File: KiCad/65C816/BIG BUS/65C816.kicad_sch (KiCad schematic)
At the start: 34 parts, among them J1 Displays, J2 Serial I/O, J3 Bus Header, J4 Bus Header, J5 Bus Header, J6 Bus Header, J7 Bus Header, J8 Bus Header, J9 PWR IN, SW2 RESET, SW3 PWR_ON, U1 W65C816SxP, U10 74LS109, U2 HM62256BLP, U3 74HC00, U4 28C256, U5 ATF16V8B, U6 74HC245, U7 74LS573, U8 NE555P, U9 74LS109, Y1 16MHz

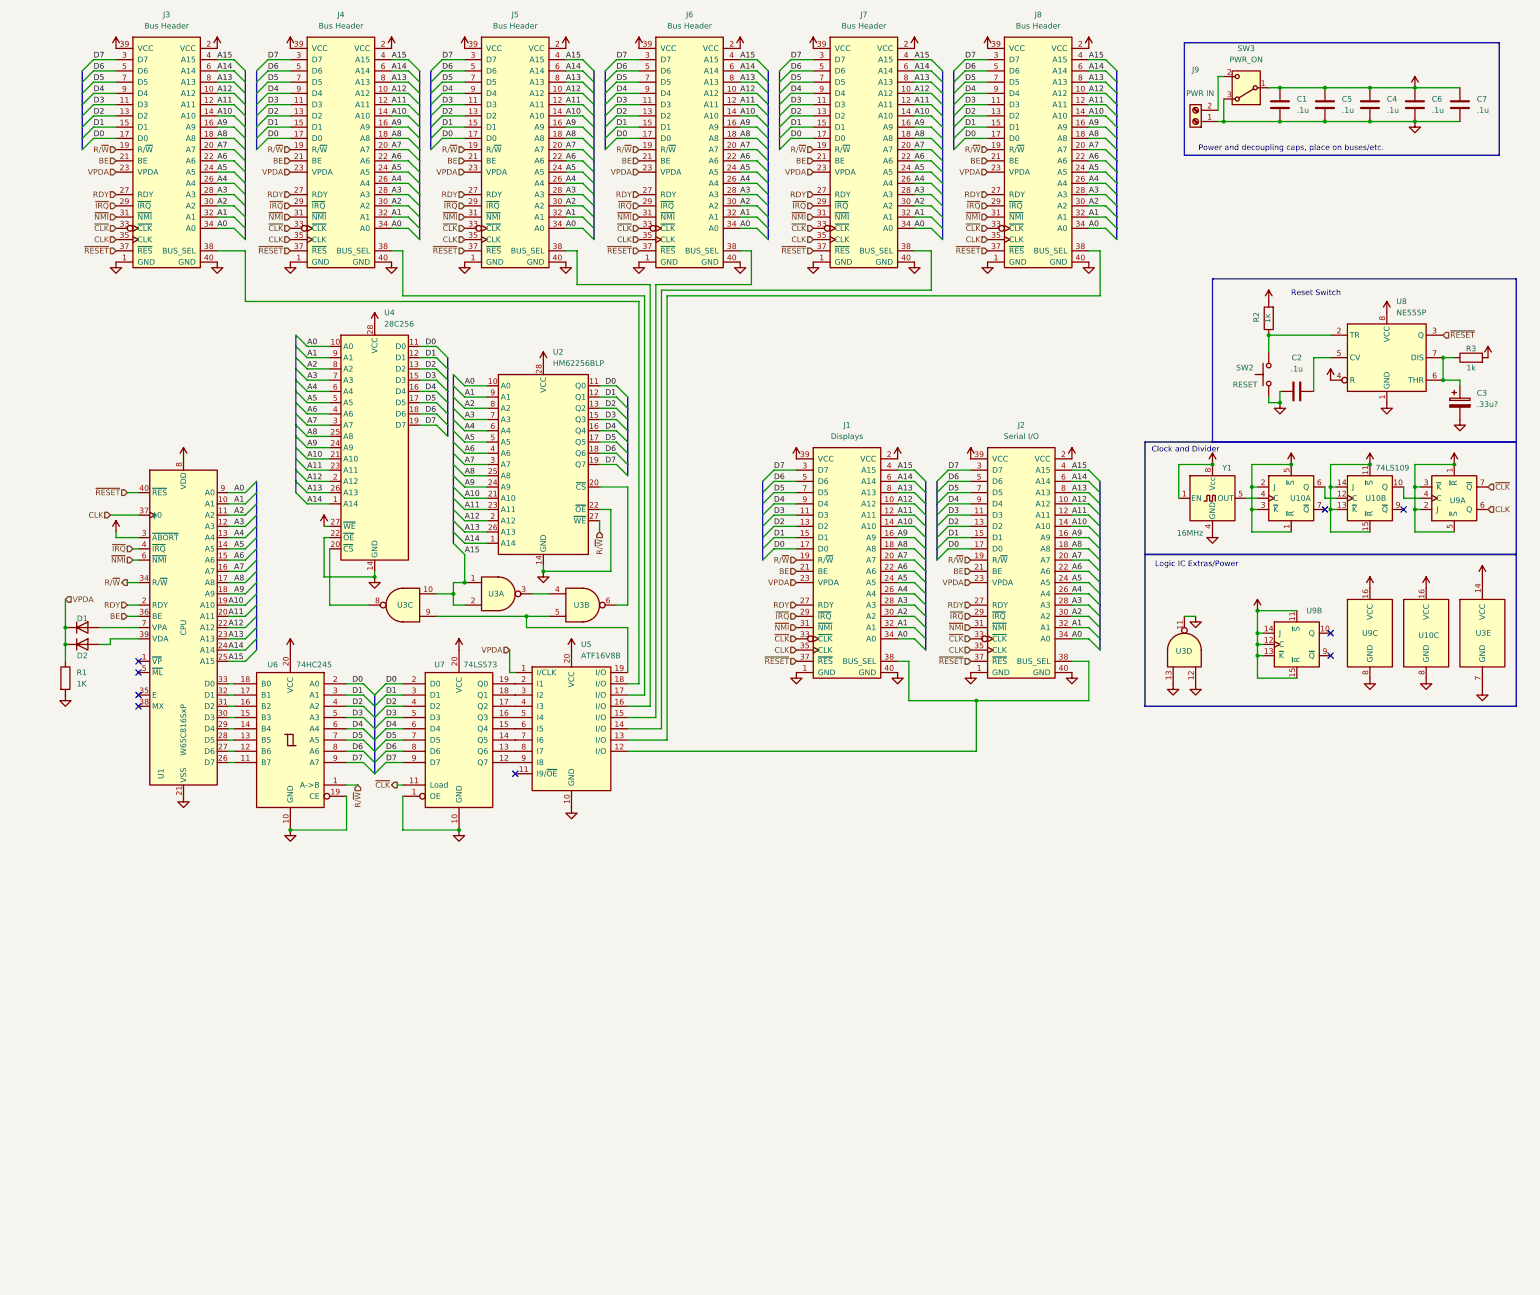
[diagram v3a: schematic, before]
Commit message: Schematic updates
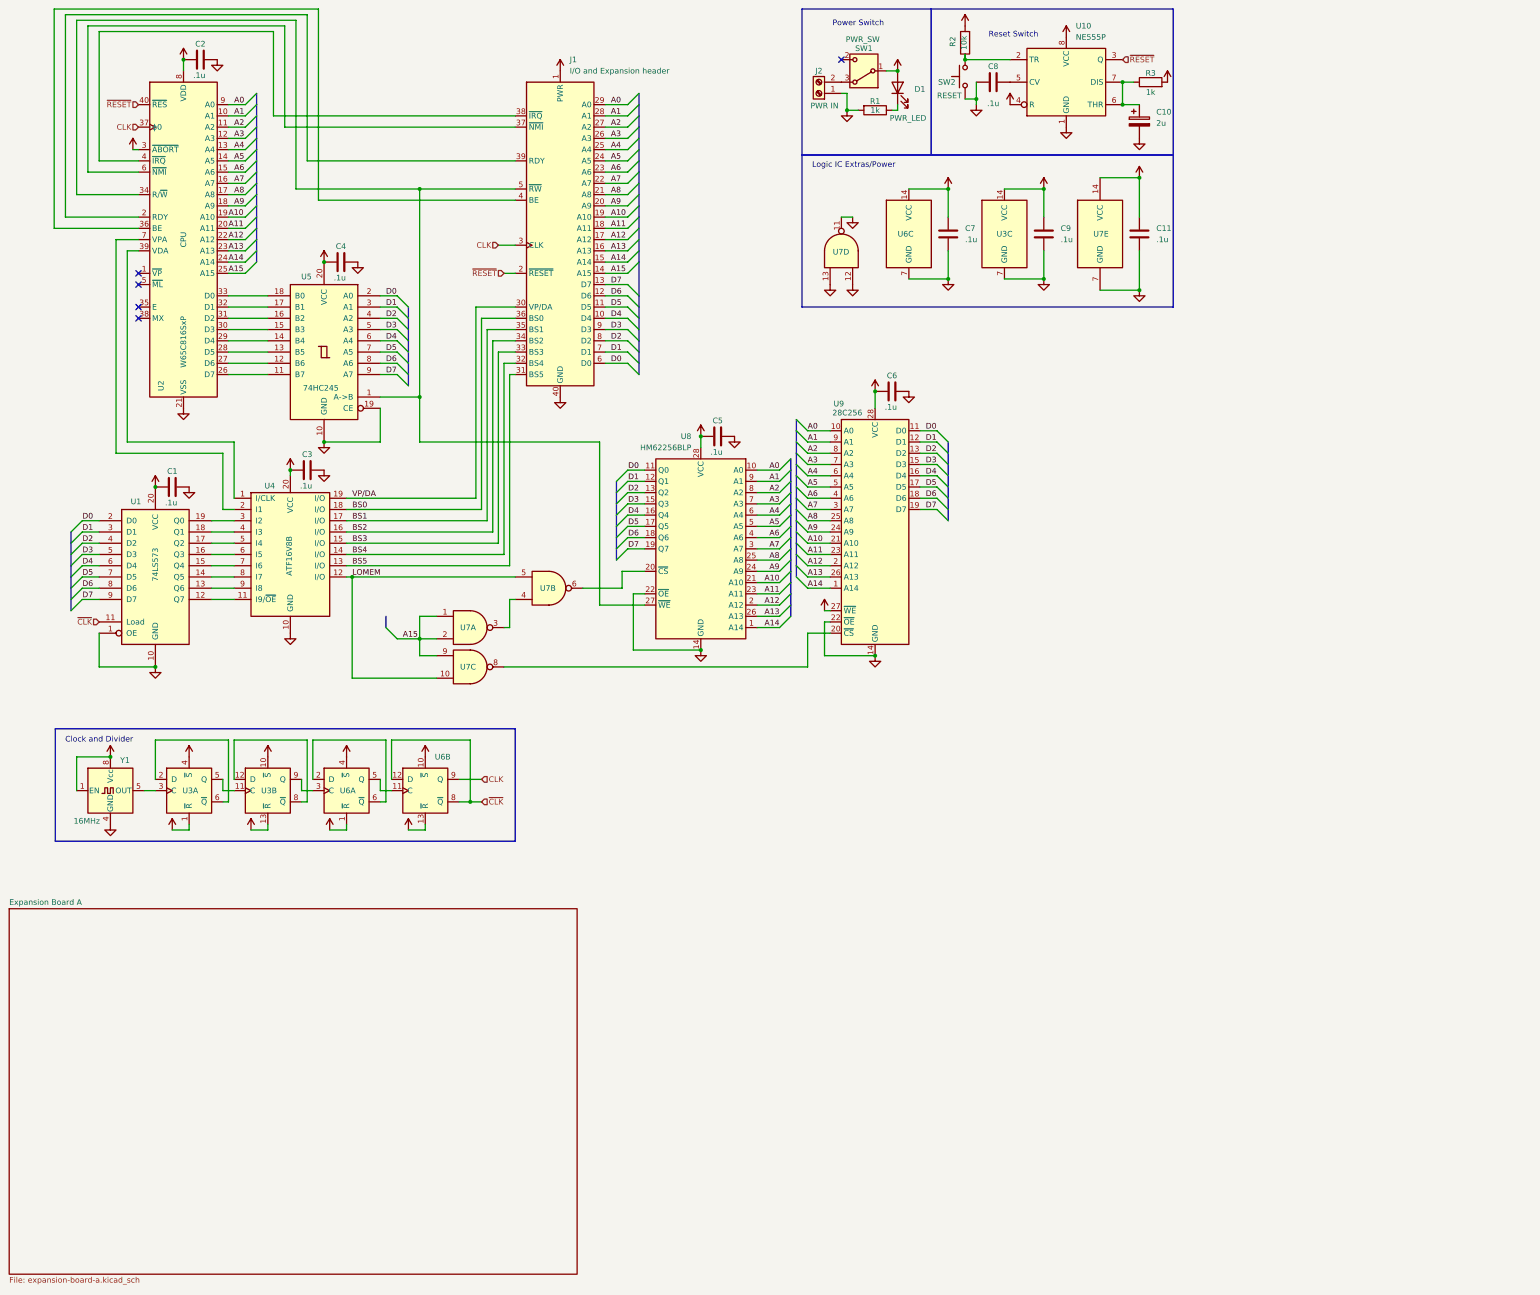
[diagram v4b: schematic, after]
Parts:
- removed D1, D2: D, Diode_THT:D_A-405_P7.62mm_Horizontal, symbol Device:D
- removed J1: Displays, Connector_IDC:IDC-Header_2x20_P2.54mm_Vertical, symbol Board Connectors:Board_Bus_V2
- removed J2: Serial I/O, Connector_IDC:IDC-Header_2x20_P2.54mm_Vertical, symbol Board Connectors:Board_Bus_V2
- removed J3, J4, J5, J6, J7, J8: Bus Header, Connector_IDC:IDC-Header_2x20_P2.54mm_Vertical, symbol Board Connectors:Board_Bus_V2
- removed U10, U9: 74LS109, Package_DIP:DIP-16_W7.62mm_Socket, symbol 74xx:74LS109
- removed unit 3 of U3
- removed unit 1 of U3
- added C11, C2, C3, C9: .1u, Capacitor_THT:C_Disc_D3.4mm_W2.1mm_P2.50mm, symbol Device:C
- added D1: PWR_LED, LED_THT:LED_D5.0mm, symbol Device:LED
- added J1: I/O and Expansion header, Connector_PinHeader_2.54mm:PinHeader_2x20_P2.54mm_Vertical, symbol Board Connectors:Bus_Connector
- added U3, U6: 74HC74, Package_DIP:DIP-14_W7.62mm_Socket, symbol 74xx:74HC74
- added unit 3 of U7
- added unit 1 of U7
- C1, C4, C5, C6: footprint Capacitor_THT:C_Disc_D3.0mm_W2.0mm_P2.50mm -> Capacitor_THT:C_Disc_D3.4mm_W2.1mm_P2.50mm; Note Place at least 1 per board? -> (none)
- C10: renamed from C3; value .33u? -> 2u
- C7: footprint Capacitor_THT:C_Disc_D3.0mm_W2.0mm_P2.50mm -> Capacitor_THT:C_Disc_D3.4mm_W2.1mm_P2.50mm
- R1: value 1K -> 1k; footprint Resistor_THT:R_Axial_DIN0204_L3.6mm_D1.6mm_P7.62mm_Horizontal -> Resistor_THT:R_Axial_DIN0207_L6.3mm_D2.5mm_P10.16mm_Horizontal
- R2: value 1k -> 10k; footprint Resistor_THT:R_Axial_DIN0204_L3.6mm_D1.6mm_P7.62mm_Horizontal -> Resistor_THT:R_Axial_DIN0207_L6.3mm_D2.5mm_P10.16mm_Horizontal
- R3: footprint Resistor_THT:R_Axial_DIN0204_L3.6mm_D1.6mm_P7.62mm_Horizontal -> Resistor_THT:R_Axial_DIN0207_L6.3mm_D2.5mm_P10.16mm_Horizontal
- SW1: renamed from SW3; value PWR_ON -> PWR_SW
- renumbered C2 to C8, J9 to J2, U7 to U1, U8 to U10, U1 to U2, U5 to U4, U6 to U5, U3 to U7, U2 to U8, U4 to U9
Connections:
- net +5V: now also C11.1, C2.1, C3.1, C9.1, D1.2 (A), J1.1 (PWR), U3.1 (~{R}), U3.10 (~{S}), U3.13 (~{R}), U3.14 (VCC), U3.4 (~{S}), U6.1 (~{R}), U6.10 (~{S}), U6.13 (~{R}), U6.14 (VCC), U6.4 (~{S})
- net A0: now also J1.29 (A0)
- net A1: now also J1.28 (A1)
- net A10: now also J1.19 (A10)
- net A11: now also J1.18 (A11)
- net A12: now also J1.17 (A12)
- net A13: now also J1.16 (A13)
- net A14: now also J1.15 (A14)
- net A15: now also J1.14 (A15), U7.1, U7.2, U7.9
- net A2: now also J1.27 (A2)
- net A3: now also J1.26 (A3)
- net A4: now also J1.25 (A4)
- net A5: now also J1.24 (A5)
- net A6: now also J1.23 (A6)
- net A7: now also J1.22 (A7)
- net A8: now also J1.21 (A8)
- net A9: now also J1.20 (A9)
- net CLK: now also J1.3 (CLK), U6.9 (Q)
- net D0: now also J1.6 (D0)
- net D1: now also J1.7 (D1)
- net D2: now also J1.8 (D2)
- net D3: now also J1.9 (D3)
- net D4: now also J1.10 (D4)
- net D5: now also J1.11 (D5)
- net D6: now also J1.12 (D6)
- net D7: now also J1.13 (D7)
- net GND: now also C11.2, C2.2, C3.2, C9.2, J1.40 (GND), U3.7 (GND), U6.7 (GND); no longer SW1.3 (A)
- net ~{CLK}: now also U6.12 (D), U6.8 (~{Q})
- net ~{RESET}: now also J1.2 (~{RESET})
- net LOMEM: now reaches U4.12 (I/O)
- net LOMEM: now also U7.5, U7.10
- net at U9.20 (~{CS}): now also U7.8
- net VP/DA: now reaches U4.19 (I/O)
- net VP/DA: now also J1.30 (VP/DA); no longer U7.5
- net at U7.4: now also U7.3
- net BS2: now reaches U4.16 (I/O)
- net BS2: now also J1.34 (BS2)
- net at J2.2 (Pin_2): now also SW1.3 (A); no longer SW1.2 (C)
- net at U2.39 (VDA): now also U4.1 (I/CLK)
- net at U2.7 (VPA): now also U4.2 (I1)
- net BS4: now reaches U4.14 (I/O)
- net BS4: now also J1.32 (BS4)
- net BS1: now reaches U4.17 (I/O)
- net BS1: now also J1.35 (BS1)
- net at U1.12 (Q7): now also U4.11 (I9/~{OE}); no longer U4.9 (I8)
- net at U1.13 (Q6): now also U4.9 (I8); no longer U4.8 (I7)
- net at U1.14 (Q5): now also U4.8 (I7); no longer U4.7 (I6)
- net at U1.15 (Q4): now also U4.7 (I6); no longer U4.6 (I5)
- net at U1.16 (Q3): now also U4.6 (I5); no longer U4.5 (I4)
- net at U1.17 (Q2): now also U4.5 (I4); no longer U4.4 (I3)
- net at U1.18 (Q1): now also U4.4 (I3); no longer U4.3 (I2)
- net at U1.19 (Q0): now also U4.3 (I2); no longer U4.2 (I1)
- net BS0: now reaches U4.18 (I/O)
- net BS0: now also J1.36 (BS0)
- net BS3: now reaches U4.15 (I/O)
- net BS3: now also J1.33 (BS3)
- net at Y1.5 (OUT): now also U3.3 (C)
- net BS5: now reaches U4.13 (I/O)
- net BS5: now also J1.31 (BS5)
- net BE: no longer names the net of U2.36 (BE)
- net BE: now also J1.4 (BE)
- net RDY: no longer names the net of U2.2 (RDY)
- net RDY: now also J1.39 (RDY)
- net R/~{W}: no longer names the net of U2.34 (R/~{W}), U5.1 (A->B), U8.27 (~{WE})
- net R/~{W}: now also J1.5 (~{RW})
- net VPDA: no longer names the net of R1.1
- net VPDA: now also D1.1 (K); no longer U4.1 (I/CLK)
- net ~{IRQ}: no longer names the net of U2.4 (~{IRQ})
- net ~{IRQ}: now also J1.38 (~{IRQ})
- net ~{NMI}: no longer names the net of U2.6 (~{NMI})
- net ~{NMI}: now also J1.37 (~{NMI})
- new net: U6.11 (C), U6.5 (Q)
- new net: U6.2 (D), U6.6 (~{Q})
- new net: U3.9 (Q), U6.3 (C)
- new net: U3.2 (D), U3.6 (~{Q})
- new net: U3.11 (C), U3.5 (Q)
- new net: U3.12 (D), U3.8 (~{Q})
- no-connect marks 9 -> 5
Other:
- added sheet Expansion Board A (expansion-board-a.kicad_sch)
- note added: "Power Switch"
- note removed: "Power and decoupling caps, place on buses/etc."
- moved on the sheet: C10, C8, J2, R2, R3, SW1, SW2, U1, U10, U2, U4, U5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
